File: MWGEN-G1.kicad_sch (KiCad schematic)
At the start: 75 parts, among them J101 Conn_02x25_Odd_Even, Q101 BSS138, Q102 BSS138

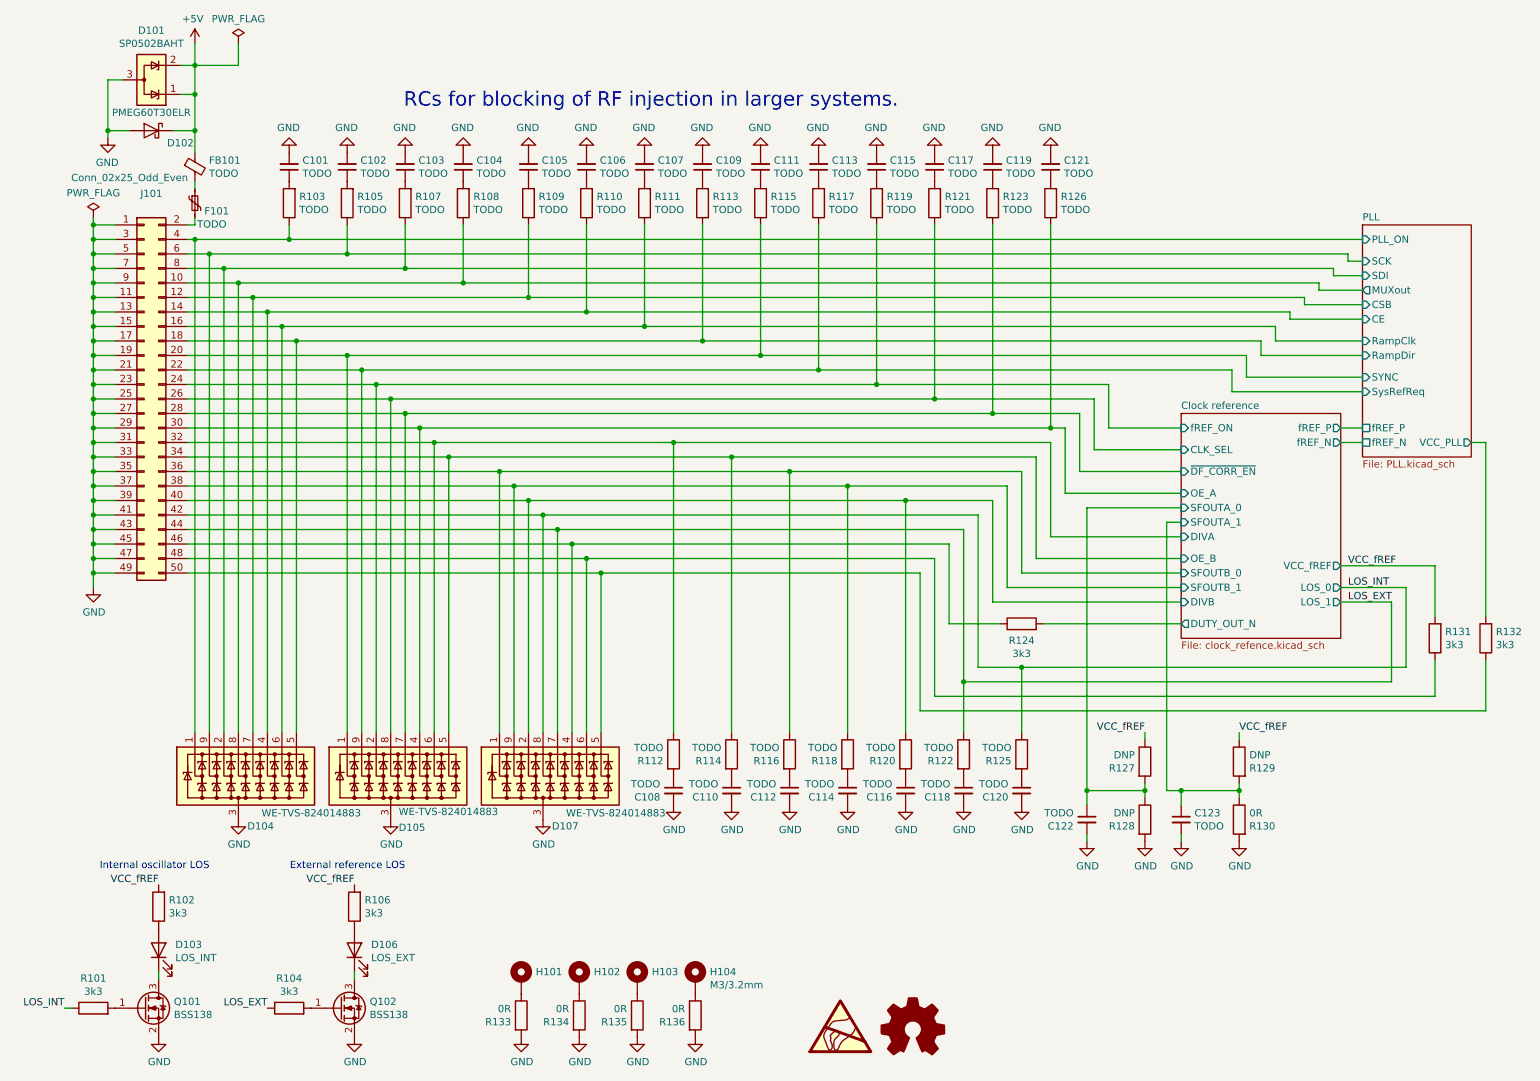
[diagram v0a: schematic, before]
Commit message: Working on making the original module a self-contained module with MCU. Added PCB.
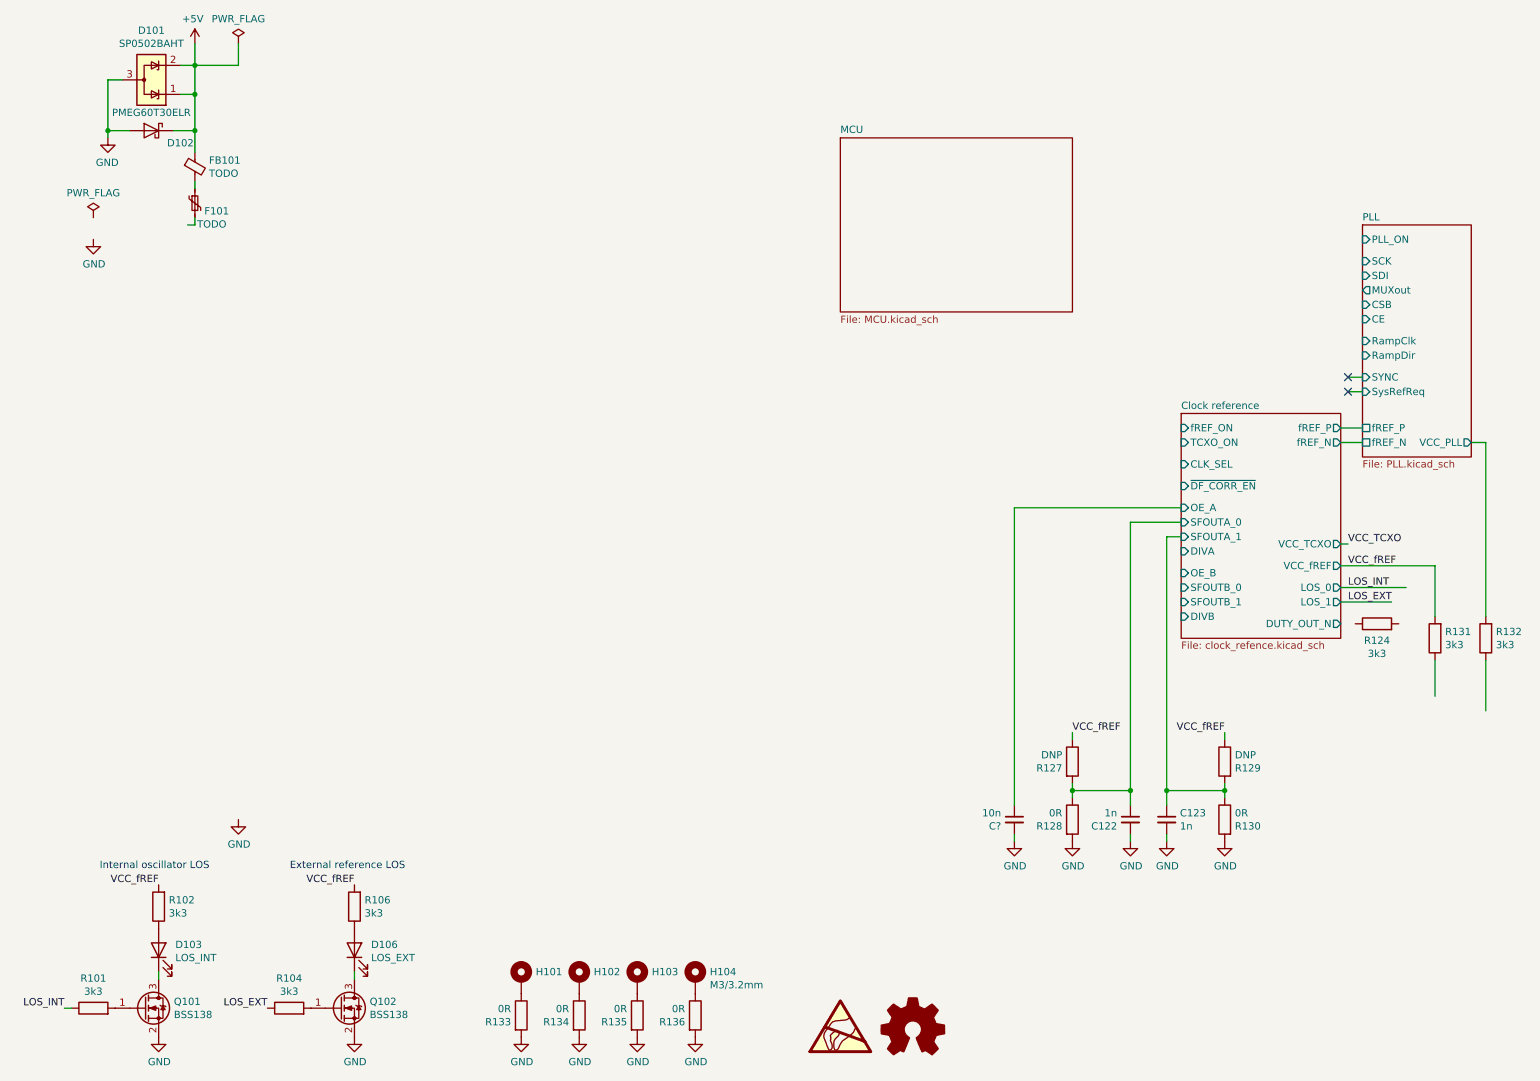
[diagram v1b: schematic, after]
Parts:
- removed C101, C102, C103, C104, C105, C106, C107, C108, C109, C110, C111, C112, C113, C114, C115, C116, C117, C118, C119, C120, C121: TODO, Capacitor_SMD:C_0603_1608Metric_Pad1.08x0.95mm_HandSolder, symbol Device:C_Small
- removed D104, D105, D107: WE-TVS-824014883, Package_DFN_QFN:UDFN-9_1.0x3.8mm_P0.5mm, symbol petr_lib_nightly:WE-TVS-824014883
- removed J101: Conn_02x25_Odd_Even, Connector_Multicomp:Multicomp_MC9A12-5034_2x25_P2.54mm_Vertical, symbol Connector_Generic:Conn_02x25_Odd_Even
- removed R103, R105, R107, R108, R109, R110, R111, R112, R113, R114, R115, R116, R117, R118, R119, R120, R121, R122, R123, R125, R126: TODO, Resistor_SMD:R_0603_1608Metric_Pad0.98x0.95mm_HandSolder, symbol Device:R
- added C?: 10n, Capacitor_SMD:C_0603_1608Metric_Pad1.08x0.95mm_HandSolder, symbol Device:C_Small
- C122, C123: value TODO -> 1n
- R128: value DNP -> 0R
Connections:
- net Clock reference/DUTY_OUT_N: no longer R124.2
- net Clock reference/OE_A: now also C?.1
- net GND: now also C?.2
- no-connect marks 0 -> 2
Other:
- added sheet MCU (MCU.kicad_sch)
- sheet Clock reference ports: added TCXO_ON, VCC_TCXO, ~{DF_CORR_EN}; removed ~DF_CORR_EN
- note removed: "RCs for blocking of RF injection in larger systems."
- moved on the sheet: C122, C123, R124, R127, R128, R129, R130

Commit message: Updates to schematic
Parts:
- removed R124: 3k3, Resistor_SMD:R_0603_1608Metric_Pad0.98x0.95mm_HandSolder, symbol Device:R
- added J?: Conn_01x02, symbol Connector_Generic:Conn_01x02
- added R? (x3): 3k, Resistor_SMD:R_0603_1608Metric_Pad0.98x0.95mm_HandSolder, symbol Device:R
- added R? (x2): 10k, Resistor_SMD:R_0603_1608Metric_Pad0.98x0.95mm_HandSolder, symbol Device:R
- added R?: 300, Resistor_SMD:R_0603_1608Metric_Pad0.98x0.95mm_HandSolder, symbol Device:R
- R102, R106: value 3k3 -> 2k
- R131, R132: value 3k3 -> 300
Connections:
- net GND: now also J?.1 (Pin_1), R?.1, R?.1, R?.1, R?.1, R?.1
- net LOS_EXT: now also R?.2
- net LOS_INT: now also R?.2
- net VCC_TCXO: now also R?.2
- net MCU/VCC_PLL: now reaches R132.1
- net MCU/VCC_PLL: now also R?.2
- net MCU/VCC_fREF: now reaches R131.1
- net MCU/VCC_fREF: now also R?.2
- net at F101.2: now also J?.2 (Pin_2)
- new net MCU/VCC_TCXO: R?.1, R?.2
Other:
- sheet MCU ports: added CE, CLK_SEL, CSB, DIVA, DIVB, DUTY, LOS_0, LOS_1, MUXout, OE_B, PLL_ON, RampClk, RampDir, SCK, SDI, SFOUTB_0, SFOUTB_1, TCXO_ON, VCC_PLL, VCC_TCXO, VCC_fREF, fREF_ON, ~{DF_CORR_EN}; removed none
- moved on the sheet: C122, C123, C?, D101, D102, D103, D106, F101, FB101, Q101, Q102, R101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

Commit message: Updated schematics
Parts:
- C?: value 10n -> 100n
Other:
- moved on the sheet: D101, D102, F101, FB101, J?

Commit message: Finished schematics
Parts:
- gave numbers to parts that had none: 8

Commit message: Schematic checked. All footprints assigned. Electrolytics need footprint check, so do the RS485 and power connectors and the MuRata oscillator (also it is now EOL) and the crystal. The power protection transils on aux input/output need replacement. PCB in sync with SCH.
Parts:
- J101: footprint (none) -> Connector_Phoenix_MSTB:PhoenixContact_MSTBA_2,5_2-G-5,08_1x02_P5.08mm_Horizontal
